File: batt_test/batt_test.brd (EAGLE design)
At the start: 50.5 x 44.5 mm, 21 parts, among them U1 PHOTON, U2 1101M2S3CQE2

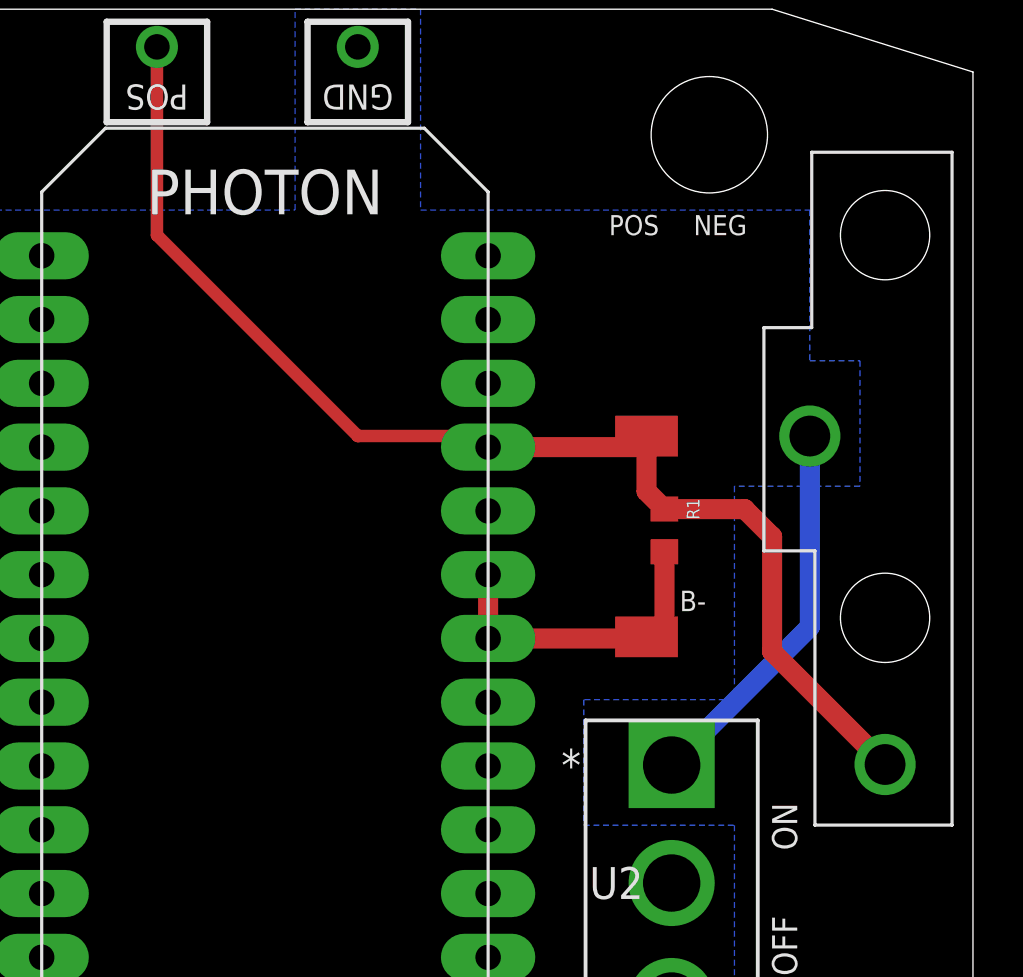
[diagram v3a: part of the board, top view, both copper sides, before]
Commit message: new contacts and bom
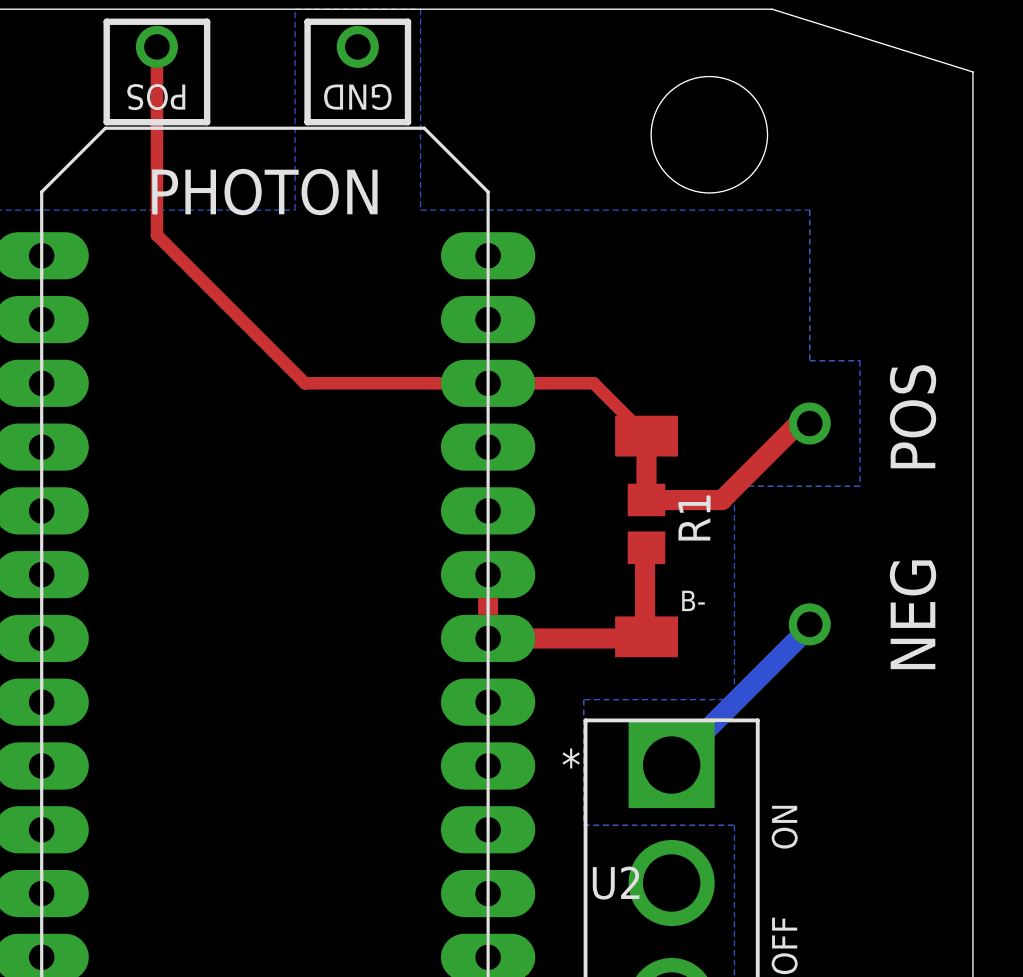
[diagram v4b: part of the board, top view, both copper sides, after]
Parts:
- removed B1: 2020COINCELL, scono:20MMCOINCELL
- added TP1, TP3: TEST_POINTTHRU, scono:TEST_POINT
- R1: device scono:R0603 -> scono:R0805
- moved R1 0.76 mm to (37.5, 24.0)
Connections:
- net B+: now also TP1.1, U1.A2; no longer B1.POS, U1.A3
- net N$1: now also TP3.1; no longer B1.NEG
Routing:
- net B+: track 49.6 -> 40.7 mm
- net N$1: track 15.4 -> 7.88 mm
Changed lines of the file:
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@@
 <?xml version="1.0" encoding="utf-8"?>
 <!DOCTYPE eagle SYSTEM "eagle.dtd">
-<eagle version="9.3.2">
+<eagle version="9.4.0">
 <drawing>
 <settings>
@@
 Board Design - S. Ono
 Battery Testing Board</text>
-<text x="41.5" y="35.5" size="0.8" layer="21" font="vector" align="bottom-right">NEG</text>
 <text x="18" y="41.5" size="1" layer="21" font="vector" rot="SR180" align="bottom-center">POS</text>
 <text x="26" y="41.5" size="1" layer="21" font="vector" rot="SR180" align="bottom-center">GND</text>
@@
 <text x="43.5" y="11" size="1" layer="21" font="vector" rot="R90">ON</text>
 <text x="43.5" y="6" size="1" layer="21" font="vector" rot="R90">OFF</text>
+<text x="49" y="26" size="1.778" layer="21" font="vector" rot="R90">POS</text>
+<text x="49" y="18" size="1.778" layer="21" font="vector" rot="R90">NEG</text>
 </plain>
 <attributes>
@@
 </autorouter>
 <elements>
-<element name="R1" library="scono" package="R0603" value="10R" x="38.21" y="23.74" smashed="yes" rot="R270">
-<attribute name="DESCRIPTION" value="RESISTOR, American symbol" x="9" y="8.5" size="1.778" layer="27" rot="R270" display="off"/>
-<attribute name="DISTRIBUTOR" value="DigiKey" x="9" y="8.5" size="1.778" layer="27" rot="R270" display="off"/>
-<attribute name="DISTRIBUTOR_PART_NUMBER" value="" x="9" y="8.5" size="1.778" layer="27" rot="R270" display="off"/>
-<attribute name="MANUFACTURER" value="Rohm Semiconductor" x="9" y="8.5" size="1.778" layer="27" rot="R270" display="off"/>
-<attribute name="MANUFACTURER_PART_NUMBER" value="" x="9" y="8.5" size="1.778" layer="27" rot="R270" display="off"/>
-<attribute name="NAME" x="39.099" y="25.01" size="0.508" layer="25" font="vector" ratio="10" rot="R270"/>
-<attribute name="NOTES" value="Cut Tape" x="9" y="8.5" size="1.778" layer="27" rot="R270" display="off"/>
-<attribute name="PACKAGE" value="R0603" x="9" y="8.5" size="1.778" layer="27" rot="R270" display="off"/>
-<attribute name="VALUE" x="37.194" y="25.01" size="0.508" layer="27" font="vector" rot="R270" align="top-left"/>
-</element>
 <element name="U1" library="scono" package="PHOTON" value="PHOTON" x="22.3" y="21.98" smashed="yes" rot="R90">
 <attribute name="NAME" x="10.243" y="2.16" size="1.27" layer="25" font="vector" ratio="7" rot="R90"/>
@@
 <attribute name="NAME" x="39.87" y="21.34" size="0.8128" layer="25" font="vector" rot="R180"/>
 </element>
-<element name="POS" library="scono" package="TEST_POINT-1206" value="TEST_POINT" x="37.5" y="27.5" smashed="yes">
-<attribute name="NAME" x="36" y="35.5" size="0.8" layer="25" font="vector"/>
-</element>
+<element name="POS" library="scono" package="TEST_POINT-1206" value="TEST_POINT" x="37.5" y="27.5" smashed="yes"/>
 <element name="U$1" library="scono" package="4-40-HOLE" value="" x="5" y="5" smashed="yes"/>
 <element name="U$3" library="scono" package="4-40-HOLE" value="" x="5" y="39.5" smashed="yes"/>
-<element name="B1" library="scono" package="20MMCOINCELL" value="2020COINCELL" x="47" y="27.5" smashed="yes" rot="R90"/>
 <element name="U$4" library="scono" package="4-40-HOLE" value="" x="40" y="39.5" smashed="yes"/>
 <element name="U2" library="scono" package="1101M2S3CQE2" value="1101M2S3CQE2" x="38.5" y="5" smashed="yes">
@@
 <element name="B+" library="scono" package="TEST_POINT" value="TEST_POINTTHRU" x="18" y="43" smashed="yes"/>
 <element name="TP2" library="scono" package="TEST_POINT" value="TEST_POINTTHRU" x="26" y="43" smashed="yes"/>
+<element name="R1" library="scono" package="R0805" value="10R" x="37.5" y="24" smashed="yes" rot="R270">
+<attribute name="NAME" x="38.77" y="25.27" size="1.27" layer="25" font="vector" ratio="10" rot="R270"/>
+<attribute name="PIE-INT-REF-NUM" value="RESISTOR-GENERIC" x="37.5" y="24" size="1.778" layer="27" rot="R270" display="off"/>
+<attribute name="VALUE" x="34.96" y="25.27" size="1.27" layer="27" font="vector" rot="R270"/>
+</element>
+<element name="TP1" library="scono" package="TEST_POINT" value="TEST_POINTTHRU" x="44" y="28" smashed="yes"/>
+<element name="TP3" library="scono" package="TEST_POINT" value="TEST_POINTTHRU" x="44" y="20" smashed="yes"/>
 </elements>
 <signals>
 <signal name="B-">
-<contactref element="R1" pad="2"/>
 <contactref element="U1" pad="A5"/>
 <contactref element="U1" pad="DAC"/>
 <contactref element="B-" pad="1"/>
-<wire x1="38.21" y1="22.89" x2="38.21" y2="20.21" width="0.8" layer="1"/>
-<wire x1="38.21" y1="20.21" x2="37.5" y2="19.5" width="0.254" layer="1"/>
 <wire x1="37.5" y1="19.5" x2="37.44" y2="19.44" width="0.254" layer="1"/>
 <wire x1="37.44" y1="19.44" x2="31.19" y2="19.44" width="0.8" layer="1"/>
 <wire x1="31.19" y1="19.44" x2="31.19" y2="21.98" width="0.8" layer="1"/>
+<contactref element="R1" pad="2"/>
+<wire x1="37.5" y1="23.05" x2="37.44" y2="22.99" width="0.8" layer="1"/>
+<wire x1="37.44" y1="22.99" x2="37.44" y2="19.44" width="0.8" layer="1"/>
 </signal>
 <signal name="B+">
-<contactref element="R1" pad="1"/>
-<contactref element="U1" pad="A3"/>
 <contactref element="POS" pad="1"/>
-<wire x1="31.19" y1="27.06" x2="37.06" y2="27.06" width="0.8" layer="1"/>
-<wire x1="37.06" y1="27.06" x2="37.5" y2="27.5" width="0.254" layer="1"/>
-<wire x1="37.5" y1="27.5" x2="37.5" y2="25.3" width="0.8" layer="1"/>
-<wire x1="37.5" y1="25.3" x2="38.21" y2="24.59" width="0.8" layer="1"/>
-<contactref element="B1" pad="POS"/>
-<wire x1="38.21" y1="24.59" x2="41.41" y2="24.59" width="0.8" layer="1"/>
-<wire x1="41.41" y1="24.59" x2="42.5" y2="23.5" width="0.8" layer="1"/>
-<wire x1="42.5" y1="23.5" x2="42.5" y2="18.919" width="0.8" layer="1"/>
-<wire x1="42.5" y1="18.919" x2="47" y2="14.419" width="0.8" layer="1"/>
 <contactref element="B+" pad="1"/>
 <wire x1="18" y1="43" x2="18" y2="35.5" width="0.5" layer="1"/>
-<wire x1="18" y1="35.5" x2="26" y2="27.5" width="0.5" layer="1"/>
-<wire x1="26" y1="27.5" x2="30.75" y2="27.5" width="0.5" layer="1"/>
-<wire x1="30.75" y1="27.5" x2="31.19" y2="27.06" width="0.5" layer="1"/>
+<contactref element="R1" pad="1"/>
+<contactref element="U1" pad="A2"/>
+<wire x1="18" y1="35.5" x2="23.9" y2="29.6" width="0.5" layer="1"/>
+<wire x1="23.9" y1="29.6" x2="31.19" y2="29.6" width="0.5" layer="1"/>
+<wire x1="31.19" y1="29.6" x2="35.4" y2="29.6" width="0.5" layer="1"/>
+<wire x1="35.4" y1="29.6" x2="37.5" y2="27.5" width="0.5" layer="1"/>
+<contactref element="TP1" pad="1"/>
+<wire x1="44" y1="28" x2="43.55" y2="28" width="0.8" layer="1"/>
+<wire x1="43.55" y1="28" x2="40.5" y2="24.95" width="0.8" layer="1"/>
+<wire x1="37.5" y1="27.5" x2="37.5" y2="25" width="0.8" layer="1"/>
+<wire x1="37.5" y1="25" x2="37.5" y2="24.95" width="0.8" layer="1"/>
+<wire x1="37.5" y1="24.95" x2="37.55" y2="24.95" width="0.8" layer="1"/>
+<wire x1="37.55" y1="24.95" x2="40.5" y2="24.95" width="0.8" layer="1"/>
+<wire x1="37.55" y1="24.95" x2="37.5" y2="25" width="0.8" layer="1"/>
 </signal>
 <signal name="GND">
@@
 </signal>
 <signal name="N$1">
-<contactref element="B1" pad="NEG"/>
 <contactref element="U2" pad="1"/>
-<wire x1="38.5" y1="14.398" x2="44.0028" y2="19.9008" width="0.8" layer="16"/>
-<wire x1="44.0028" y1="19.9008" x2="44.0028" y2="27.5" width="0.8" layer="16"/>
+<wire x1="44.0028" y1="19.9008" x2="38.5" y2="14.398" width="0.8" layer="16"/>
+<contactref element="TP3" pad="1"/>
+<wire x1="44" y1="20" x2="44.0028" y2="19.9972" width="0.8" layer="16"/>
+<wire x1="44.0028" y1="19.9972" x2="44.0028" y2="19.9008" width="0.8" layer="16"/>
 </signal>
 </signals>

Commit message: one last time?
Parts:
- added B-2: TEST_POINTTHRU, scono:TEST_POINT
- moved B+ 2.50 mm to (15.5, 43.0)
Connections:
- net B-: now also B-2.1
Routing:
- net B-: track 12.5 -> 42.3 mm
- net B+: track 40.7 -> 41.7 mm
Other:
- board text added: "B+"
- board text added: "B-"
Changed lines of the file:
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@@
 <?xml version="1.0" encoding="utf-8"?>
 <!DOCTYPE eagle SYSTEM "eagle.dtd">
-<eagle version="9.4.0">
+<eagle version="9.5.2">
 <drawing>
 <settings>
-<setting alwaysvectorfont="no"/>
+<setting alwaysvectorfont="yes"/>
 <setting verticaltext="up"/>
 </settings>
@@
 Board Design - S. Ono
 Battery Testing Board</text>
-<text x="18" y="41.5" size="1" layer="21" font="vector" rot="SR180" align="bottom-center">POS</text>
+<text x="15.5" y="41.5" size="1" layer="21" font="vector" rot="SR180" align="bottom-center">B+</text>
 <text x="26" y="41.5" size="1" layer="21" font="vector" rot="SR180" align="bottom-center">GND</text>
-<wire x1="16" y1="44" x2="16" y2="40" width="0.254" layer="21"/>
-<wire x1="16" y1="40" x2="20" y2="40" width="0.254" layer="21"/>
-<wire x1="20" y1="40" x2="20" y2="44" width="0.254" layer="21"/>
-<wire x1="20" y1="44" x2="16" y2="44" width="0.254" layer="21"/>
+<wire x1="13.5" y1="44" x2="13.5" y2="40" width="0.254" layer="21"/>
+<wire x1="13.5" y1="40" x2="17.5" y2="40" width="0.254" layer="21"/>
+<wire x1="17.5" y1="40" x2="17.5" y2="44" width="0.254" layer="21"/>
+<wire x1="17.5" y1="44" x2="13.5" y2="44" width="0.254" layer="21"/>
 <wire x1="24" y1="44" x2="28" y2="44" width="0.254" layer="21"/>
 <wire x1="28" y1="44" x2="28" y2="40" width="0.254" layer="21"/>
@@
 <text x="49" y="26" size="1.778" layer="21" font="vector" rot="R90">POS</text>
 <text x="49" y="18" size="1.778" layer="21" font="vector" rot="R90">NEG</text>
+<text x="20.5" y="41.5" size="1" layer="21" rot="SR180" align="bottom-center">B-</text>
+<wire x1="22.5" y1="44" x2="18.5" y2="44" width="0.254" layer="21"/>
+<wire x1="18.5" y1="44" x2="18.5" y2="40" width="0.254" layer="21"/>
+<wire x1="22.5" y1="40" x2="22.5" y2="44" width="0.254" layer="21"/>
+<wire x1="18.5" y1="40" x2="22.5" y2="40" width="0.254" layer="21"/>
 </plain>
 <attributes>
@@
 <attribute name="VENDOR" value="C&amp;K" x="38.5" y="5" size="1.778" layer="27" display="off"/>
 </element>
-<element name="B+" library="scono" package="TEST_POINT" value="TEST_POINTTHRU" x="18" y="43" smashed="yes"/>
+<element name="B+" library="scono" package="TEST_POINT" value="TEST_POINTTHRU" x="15.5" y="43" smashed="yes"/>
 <element name="TP2" library="scono" package="TEST_POINT" value="TEST_POINTTHRU" x="26" y="43" smashed="yes"/>
 <element name="R1" library="scono" package="R0805" value="10R" x="37.5" y="24" smashed="yes" rot="R270">
@@
 <element name="TP1" library="scono" package="TEST_POINT" value="TEST_POINTTHRU" x="44" y="28" smashed="yes"/>
 <element name="TP3" library="scono" package="TEST_POINT" value="TEST_POINTTHRU" x="44" y="20" smashed="yes"/>
+<element name="B-2" library="scono" package="TEST_POINT" value="TEST_POINTTHRU" x="20.5" y="43" smashed="yes"/>
 </elements>
 <signals>
@@
 <wire x1="37.5" y1="23.05" x2="37.44" y2="22.99" width="0.8" layer="1"/>
 <wire x1="37.44" y1="22.99" x2="37.44" y2="19.44" width="0.8" layer="1"/>
+<contactref element="B-2" pad="1"/>
+<wire x1="20.5" y1="43" x2="20.5" y2="27" width="0.5" layer="16"/>
+<wire x1="28.06" y1="19.44" x2="31.19" y2="19.44" width="0.5" layer="16"/>
+<wire x1="20.5" y1="27" x2="28.06" y2="19.44" width="0.5" layer="16"/>
 </signal>
 <signal name="B+">
 <contactref element="POS" pad="1"/>
 <contactref element="B+" pad="1"/>
-<wire x1="18" y1="43" x2="18" y2="35.5" width="0.5" layer="1"/>
+<wire x1="15.5" y1="43" x2="15.5" y2="38" width="0.5" layer="1"/>
 <contactref element="R1" pad="1"/>
 <contactref element="U1" pad="A2"/>
-<wire x1="18" y1="35.5" x2="23.9" y2="29.6" width="0.5" layer="1"/>
+<wire x1="15.5" y1="38" x2="23.9" y2="29.6" width="0.5" layer="1"/>
 <wire x1="23.9" y1="29.6" x2="31.19" y2="29.6" width="0.5" layer="1"/>
 <wire x1="31.19" y1="29.6" x2="35.4" y2="29.6" width="0.5" layer="1"/>
